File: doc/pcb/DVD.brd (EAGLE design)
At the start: 48.1 x 42.3 mm, 37 parts, among them IC2 74HC14N, IC3 7805

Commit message: PCB routed
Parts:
- moved R4 15.2 mm to (21.6, 17.8), turned to 270 degrees
- moved R3 10.2 mm to (34.3, 17.8)
- moved NRF24L01 6.35 mm to (35.6, 6.35)
- moved C4 5.08 mm to (29.2, 6.35), turned to 270 degrees
- moved JP8 3.81 mm to (43.2, 40.6)
- moved JP9 3.81 mm to (47.0, 40.6)
- moved D2 2.54 mm to (24.1, 17.8)
- moved D4 2.54 mm to (31.8, 17.8)
- moved R2 2.54 mm to (29.2, 17.8), turned to 270 degrees
- moved R5 2.54 mm to (26.7, 17.8)
- moved LED1 1.80 mm to (14.0, 29.2)
- moved C5 1.80 mm to (47.0, 5.08), turned to 0 degrees
- moved C6 1.27 mm to (16.5, 34.3), turned to 180 degrees
- turned R1 to 270 degrees
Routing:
- net GND: track 93.6 -> 5.61 mm, vias 0 -> 2
- net V+: track 57.3 -> 91.5 mm
- net N$10: track 27.1 -> 7.62 mm
- net SPEED_SENSOR: track 58.4 -> 42.7 mm
- net +3V3: track 46.3 -> 30.8 mm, vias 0 -> 1
- net JP8: track 45.5 -> 60.1 mm, vias 0 -> 1
- net N$8: track 8.89 -> 0.00 mm
- net N$11: track 19.6 -> 11.2 mm
- net N$18: track 16.8 -> 24.2 mm
- net ENGINE1: track 15.1 -> 21.0 mm
- net CE: track 13.5 -> 8.21 mm
- net CSN_RADIO: track 7.44 -> 2.54 mm
- net PWM: track 27.0 -> 22.5 mm
- net +5V: track 146.2 -> 142.0 mm
- net AGND: track 28.6 -> 32.2 mm
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
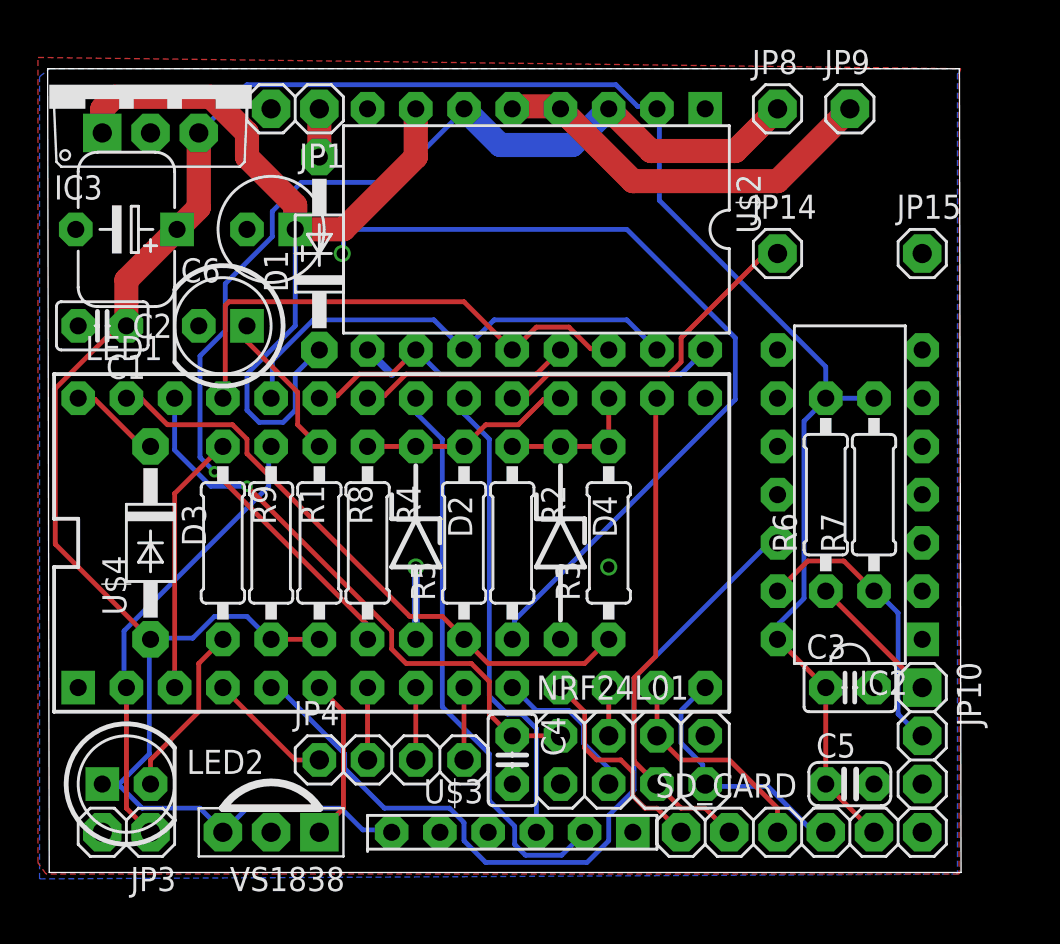
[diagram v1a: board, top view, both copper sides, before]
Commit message: PCB updates
Moved voltage regulator
Checked that the OKI switching regulator would also fit (it does)
Moved capacitors around voltage regulator
Moved motor pins but couldn't make one square
Made other pin 1 square
Added more vias to the ground copper pour
Re-loaded DRC from PCB house and made necessary changes
Increased isolation of copper pour as much as possible (0.005->0.012)
in order to sleep better :-)
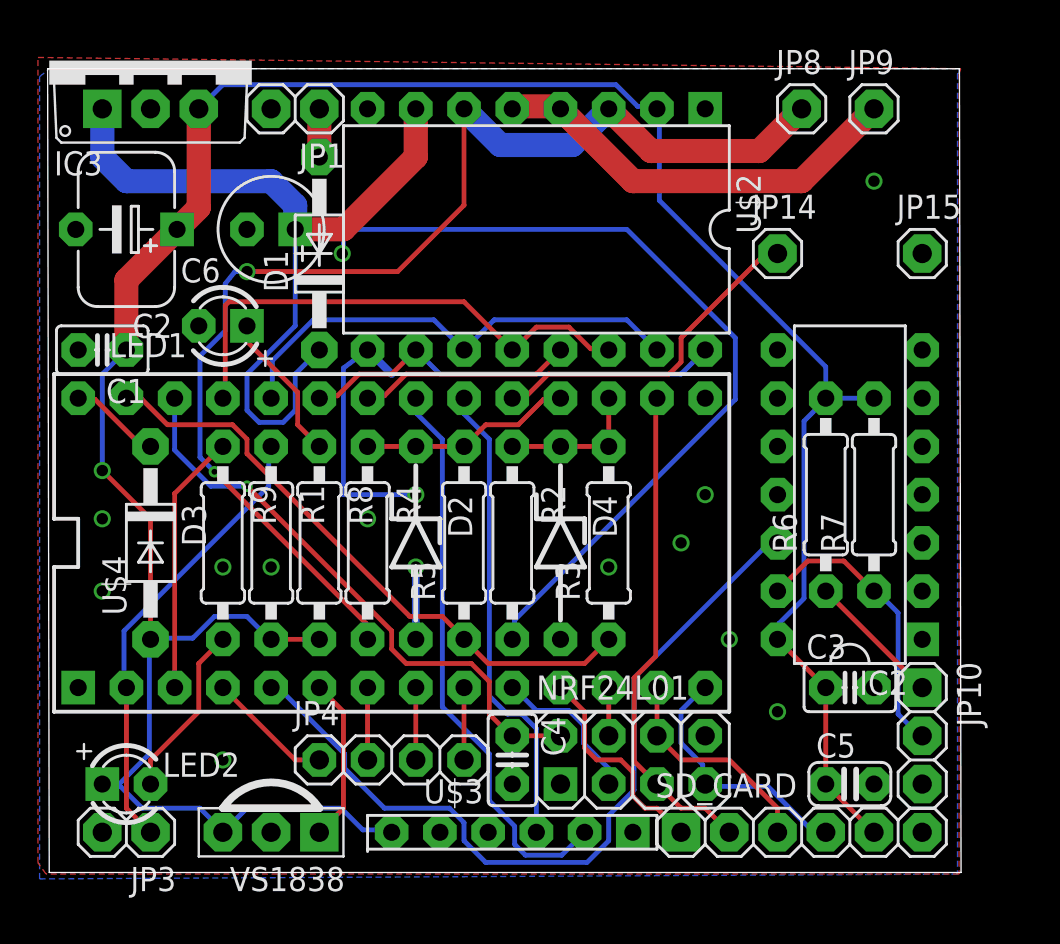
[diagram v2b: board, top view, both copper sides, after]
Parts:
- LED1, LED2: device adafruit:LED5MM -> adafruit:LED3MM
- moved IC3 1.27 mm to (10.2, 43.2)
- moved JP8 1.27 mm to (44.5, 40.6)
- moved C1 1.27 mm to (7.62, 27.9)
- moved JP9 1.27 mm to (48.3, 40.6)
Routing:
- net GND: track 5.61 -> 17.7 mm, vias 2 -> 13
- net JP8: track 60.1 -> 63.6 mm, vias 1 -> 2
- net ENGINE1: track 21.0 -> 22.3 mm
- net V+: track 91.5 -> 90.4 mm
- net +5V: track 142.0 -> 142.9 mm, vias 0 -> 1

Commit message: PCB and Schematic Updates
- Added 2-pin jumper for +5V and GND near the 4-pin header with
  spare signal pins
- Added Langloecher
- Cut the lower corners of the PCB to make it fit into the car
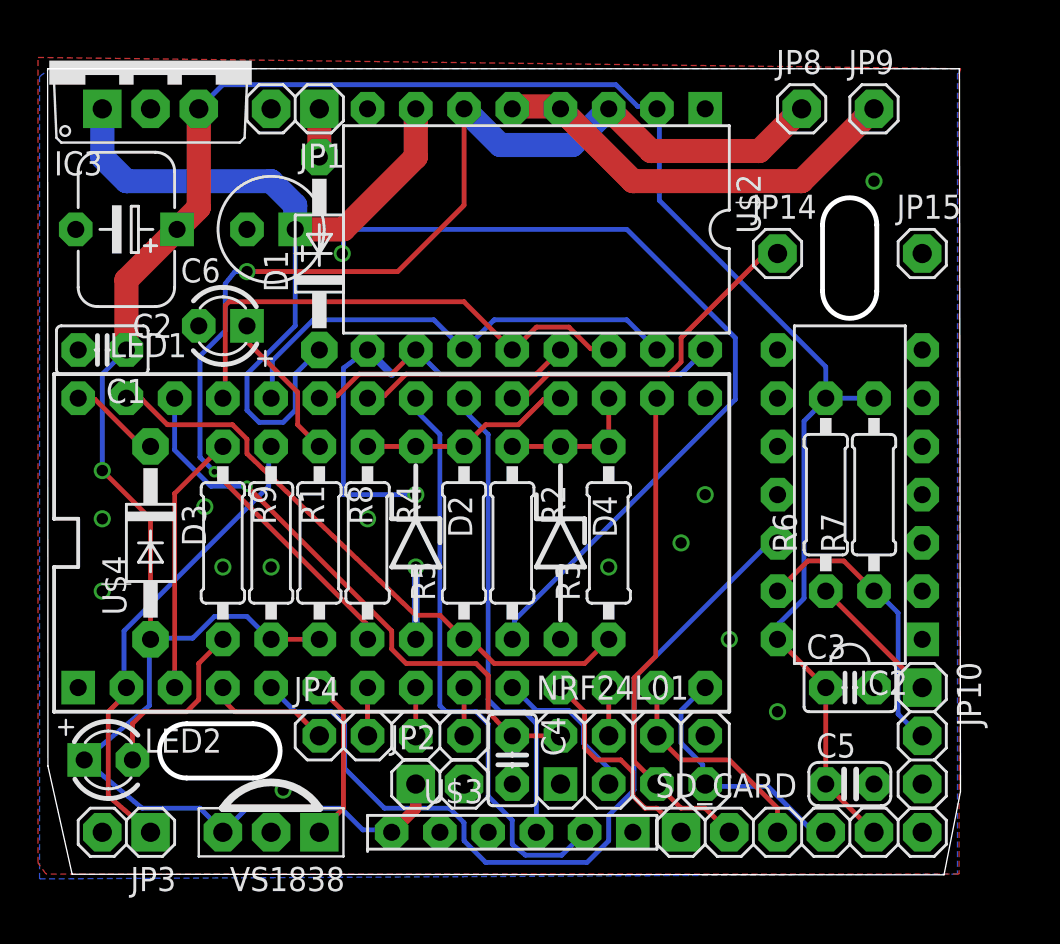
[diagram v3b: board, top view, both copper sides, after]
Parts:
- added JP2: (no value), pinhead:1X02
- moved LED2 1.59 mm to (7.94, 6.35)
- moved JP4 1.27 mm to (22.9, 7.62)
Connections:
- net +5V: now also JP2.1
- net GND: now also JP2.2
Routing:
- net +5V: track 142.9 -> 146.0 mm
- net N$3: track 3.81 -> 2.54 mm
- net N$22: track 3.81 -> 2.54 mm
- net N$21: track 3.81 -> 2.54 mm
- net SCL: track 30.1 -> 31.0 mm
- net SPEED_SENSOR: track 42.7 -> 43.6 mm
- net N$18: track 24.2 -> 25.1 mm
- net GND: vias 13 -> 15
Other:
- board size 48.1 x 42.3 mm -> 48.1 x 42.5 mm

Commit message: Silkscreen cleanup, reconnected Vin to 7805
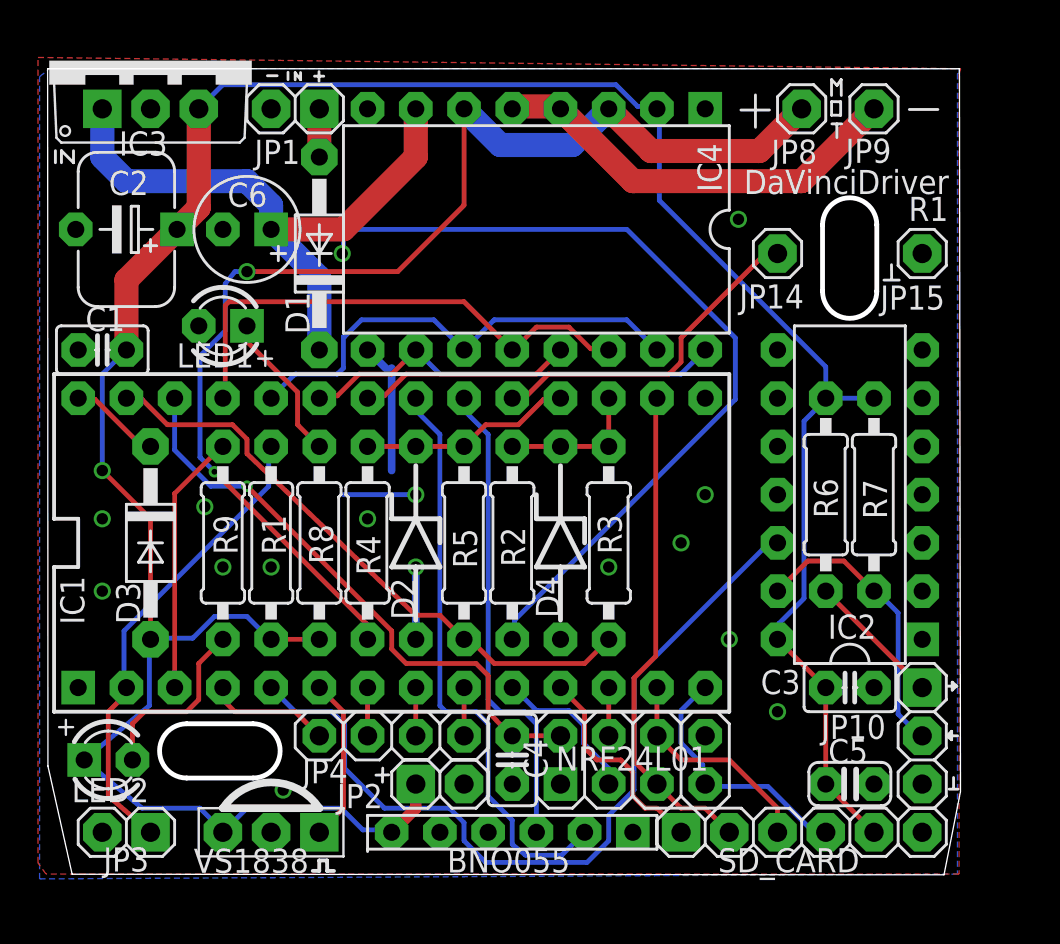
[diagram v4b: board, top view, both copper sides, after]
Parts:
- moved C6 1.27 mm to (15.2, 34.3)
- renumbered U$2 to IC4, U$3 to BNO055, U$4 to IC1
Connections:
- net GND: now also IC3.2
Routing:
- net V+: track 90.4 -> 81.8 mm
- net GND: track 17.7 -> 14.8 mm
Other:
- board text added: "DaVinciDriver"
- board text added: "R1"
